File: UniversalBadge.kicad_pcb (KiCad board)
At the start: 2 copper layers, 90 x 78.6 mm, 17 parts, among them J1 Conn_01x03_Pin, J2 Conn_01x06_Pin, J3 Conn_02x04_Counter_Clockwise, SW1 Push_Button, U1 ATTINY85-20PU

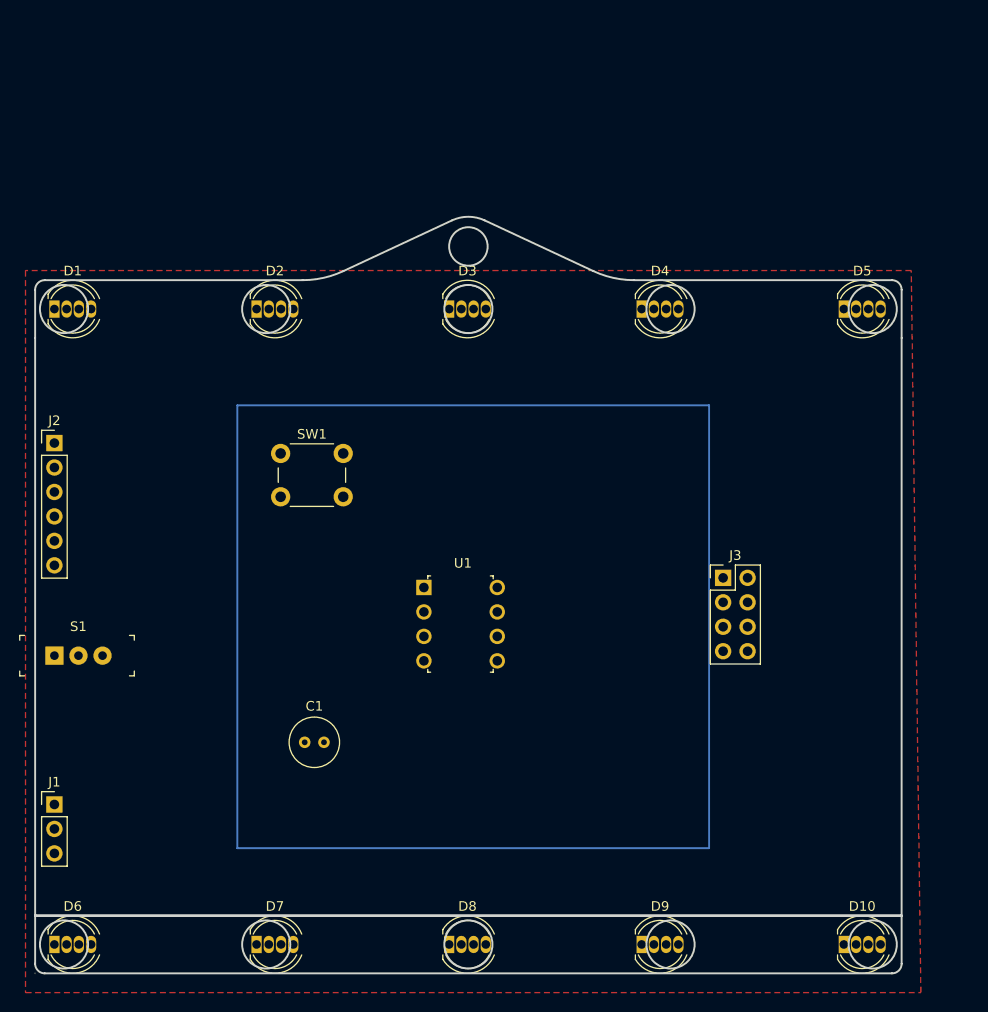
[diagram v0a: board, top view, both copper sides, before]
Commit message: redo board layout
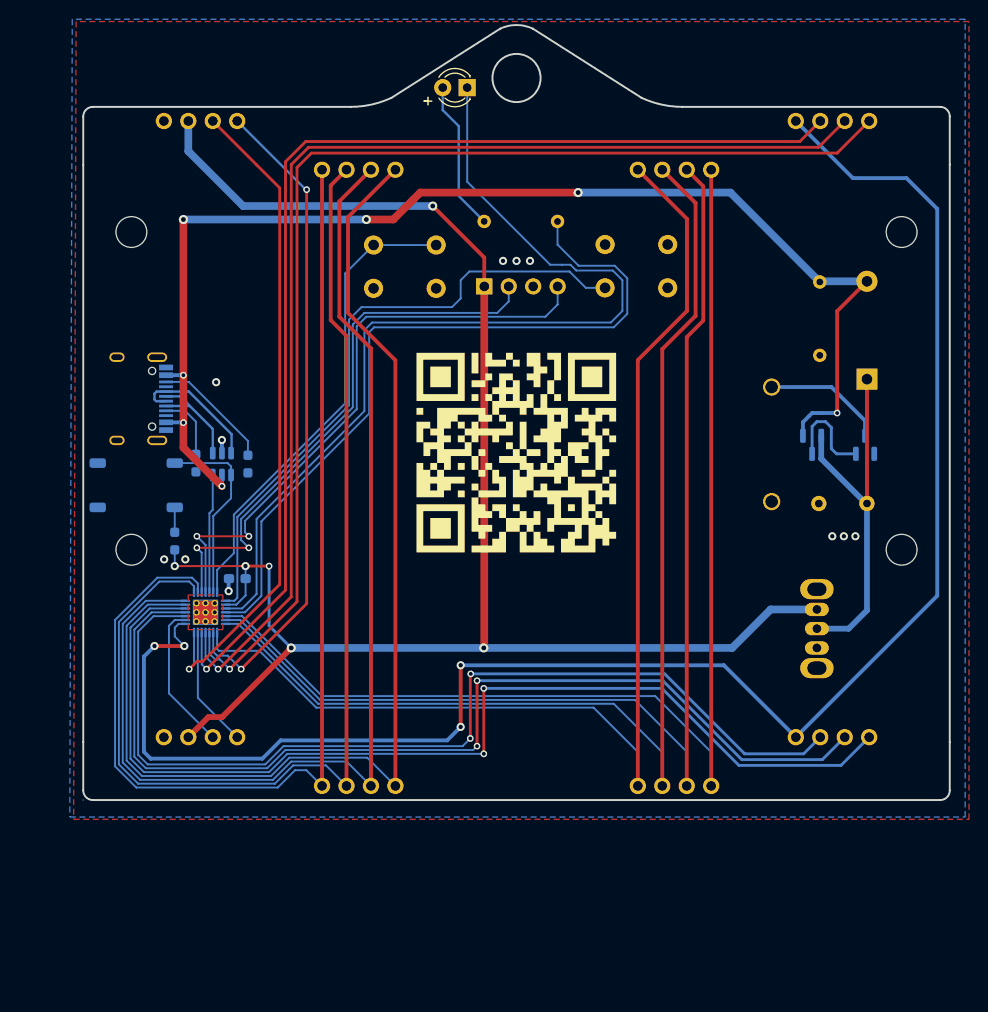
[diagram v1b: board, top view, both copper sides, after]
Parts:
- removed D10, D2, D3, D4, D5, D6, D7, D8, D9: APA-106-F5, LED_THT:LED_D5.0mm-4_RGB
- removed J1: Conn_01x03_Pin, Connector_PinHeader_2.54mm:PinHeader_1x03_P2.54mm_Vertical
- removed J2: Conn_01x06_Pin, Connector_PinHeader_2.54mm:PinHeader_1x06_P2.54mm_Vertical
- removed J3: Conn_02x04_Counter_Clockwise, Connector_PinHeader_2.54mm:PinHeader_2x04_P2.54mm_Vertical
- removed S1: EG1218, digikey-footprints:Switch_Slide_11.6x4mm_EG1218
- added BAT1: Battery, _trueControl:MYOUNG BH-AAA-Axxx024, B.Cu at (146.0, 69.0)
- added BOOT1: Push_Button, _trueControl:TactSw_Hanbo_TS-KG057S-BT34F, B.Cu at (105.5, 67.3)
- added BTN1: Push_Button, Button_Switch_THT:SW_PUSH_6mm, B.Cu at (136.7, 42.4)
- added BTN2: Push_Button, Button_Switch_THT:SW_PUSH_6mm, B.Cu at (154.2, 46.8)
- added C2: 0u1, Capacitor_SMD:C_0603_1608Metric_Pad1.08x0.95mm_HandSolder, B.Cu at (116.0, 77.0)
- added JA1: LED_Assy_Top, _trueControl:Stacking_Module_16P_REV2, F.Cu at (145.0, 32.0)
- added JA2: LED_Assy_Bot, _trueControl:Stacking_Module_16P_REV2, F.Cu at (145.0, 96.0)
- added JDBG1: Conn_01x04, Connector_PinHeader_2.54mm:PinHeader_1x04_P2.54mm_Vertical, B.Cu at (141.7, 46.6)
- added LED1: RED, LED_THT:LED_D3.0mm, F.Cu at (139.9, 26.0)
- added Q1: CJ3401, Package_TO_SOT_SMD:SOT-23, B.Cu at (181.2, 63.1)
- added Q2: CJ3401, Package_TO_SOT_SMD:SOT-23, B.Cu at (175.7, 63.1)
- added R1: 5K1, Resistor_SMD:R_0603_1608Metric_Pad0.98x0.95mm_HandSolder, B.Cu at (111.7, 65.0)
- added R2: 5K1, Resistor_SMD:R_0603_1608Metric_Pad0.98x0.95mm_HandSolder, B.Cu at (117.1, 65.1)
- added R3: 47K, Resistor_THT:R_Axial_DIN0204_L3.6mm_D1.6mm_P7.62mm_Horizontal, B.Cu at (176.5, 53.8)
- added R4: 560, Resistor_THT:R_Axial_DIN0204_L3.6mm_D1.6mm_P7.62mm_Horizontal, B.Cu at (141.6, 39.9)
- added R5: 5K1, Resistor_SMD:R_0603_1608Metric_Pad0.98x0.95mm_HandSolder, B.Cu at (109.5, 73.1)
- added REF**: MountingHole_3.2mm_M3_ISO14580, MountingHole:MountingHole_3.2mm_M3_ISO14580, F.Cu at (105.0, 41.0)
- added REF**: MountingHole_3.2mm_M3_ISO14580, MountingHole:MountingHole_3.2mm_M3_ISO14580, F.Cu at (185.0, 74.0)
- added REF**: MountingHole_3.2mm_M3_ISO14580, MountingHole:MountingHole_3.2mm_M3_ISO14580, F.Cu at (185.0, 41.0)
- added REF**: MountingHole_3.2mm_M3_ISO14580, MountingHole:MountingHole_3.2mm_M3_ISO14580, F.Cu at (105.0, 74.0)
- added U2: USBLC6-2SC6, Package_TO_SOT_SMD:SOT-23-6, B.Cu at (114.4, 65.1)
- added USB1: USB_C_Receptacle_USB2.0_14P, Connector_USB:USB_C_Receptacle_HRO_TYPE-C-31-M-12, B.Cu at (104.5, 58.3)
- C1: value C -> 10u; footprint Capacitor_THT:C_Radial_D5.0mm_H5.0mm_P2.00mm -> Capacitor_THT:C_Disc_D6.0mm_W4.4mm_P5.00mm; moved to B.Cu
- D1: value APA-106-F5 -> SB160; footprint LED_THT:LED_D5.0mm-4_RGB -> Diode_THT:D_DO-41_SOD81_P10.16mm_Horizontal; moved to B.Cu
- SW1: value Push_Button -> SK12D07VG6; footprint Button_Switch_THT:SW_PUSH_6mm -> Button_Switch_THT:SW_Slide_SPDT_Angled_CK_OS102011MA1Q; moved to B.Cu
- U1: value ATTINY85-20PU -> CH32X035G8U6; footprint digikey-footprints:DIP-8_W7.62mm -> _trueControl:QFN-28-1EP_4x4mm_P0.4mm_EP2.4x2.4mm_ThermalVias_LP; moved to B.Cu
- moved D1 84.7 mm to (181.4, 56.3), turned to 90 degrees
- moved C1 58.9 mm to (176.4, 69.2)
- moved SW1 58.0 mm to (176.2, 80.2), turned to -90 degrees
- moved U1 22.8 mm to (112.7, 80.5), turned to 180 degrees
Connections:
- net at2 renamed VCC
- C1 pad 1: at8 -> GND
- C1 pad 2: at4 -> Net-(D1-K)
- D1 pad 1: Net-(D1-DO) -> Net-(D1-K)
- D1 pad 2: at4 -> Net-(D1-A)
- SW1 pad 2: at4 -> Net-(D1-K)
- U1 pad 1: at1 -> /BTN1
- U1 pad 3: /at3 -> Net-(LED1-K)
- U1 pad 4: unconnected-(U1-GND-Pad4) -> Net-(U1-PC3)
- U1 pad 5: /at5 -> /T2C1
- U1 pad 6: /at6 -> /T2C2
- U1 pad 7: /at7 -> /T2C3
- U1 pad 8: unconnected-(U1-VCC-Pad8) -> /T2C4
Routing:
- net /T3C1: track 0.00 -> 176.7 mm, vias 0 -> 4
- net VCC: track 0.00 -> 176.3 mm, vias 0 -> 6
- net Net-(D1-A): track 0.00 -> 130.3 mm, vias 0 -> 7
- net /T2C1: track 0.00 -> 123.8 mm
- net /T2C2: track 0.00 -> 122.5 mm
- net /T2C4: track 0.00 -> 121.6 mm
- net /RGB2: track 0.00 -> 121.4 mm, vias 0 -> 1
- net /T2C3: track 0.00 -> 121.2 mm
- net /T1C1: track 0.00 -> 119.7 mm
- net /RGB3: track 0.00 -> 119.3 mm, vias 0 -> 1
- net /RGB4: track 0.00 -> 117.4 mm, vias 0 -> 1
- net /T1C2: track 0.00 -> 117.0 mm
- net /T1C3: track 0.00 -> 116.6 mm
- net /T1C4: track 0.00 -> 114.6 mm
- net /RGB10: track 0.00 -> 109.6 mm, vias 0 -> 2
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- added copper zone on B.Cu, net GND
- added copper zone on F.Cu, net GND
- removed copper zone on F.Cu, net unconnected-(U1-GND-Pad4)
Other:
- board size 90 x 78.6 mm -> 90 x 80.5 mm
- board text added: "3V"
- board text added: "ACTION"
- board text added: "BOOT"
- board text added: "CK"
- board text added: "Circuit redesign by"
- board text added: "Concept and original design by"
- board text added: "GD"
- board text added: "IO"
- board text added: "Install Battery Box HERE!"
- board text added: "MODE"
- board text added: "Modular Badge REV1 20250324"
- board text added: "OFF"
- board text added: "ON"
- board text added: "REV2 20230323"
- board text added: "Satx Circuit Makers"
- board text added: "true"
